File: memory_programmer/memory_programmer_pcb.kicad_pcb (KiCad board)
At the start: 2 copper layers, 68.6 x 53.3 mm, 22 parts, among them J1 Conn_01x03, J2 Conn_02x08_Odd_Even, J3 Conn_02x08_Odd_Even, P1 Power, P2 Analog, P3 Digital, P4 Digital, P5 CONN_01X01, P6 CONN_01X01, P7 CONN_01X01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

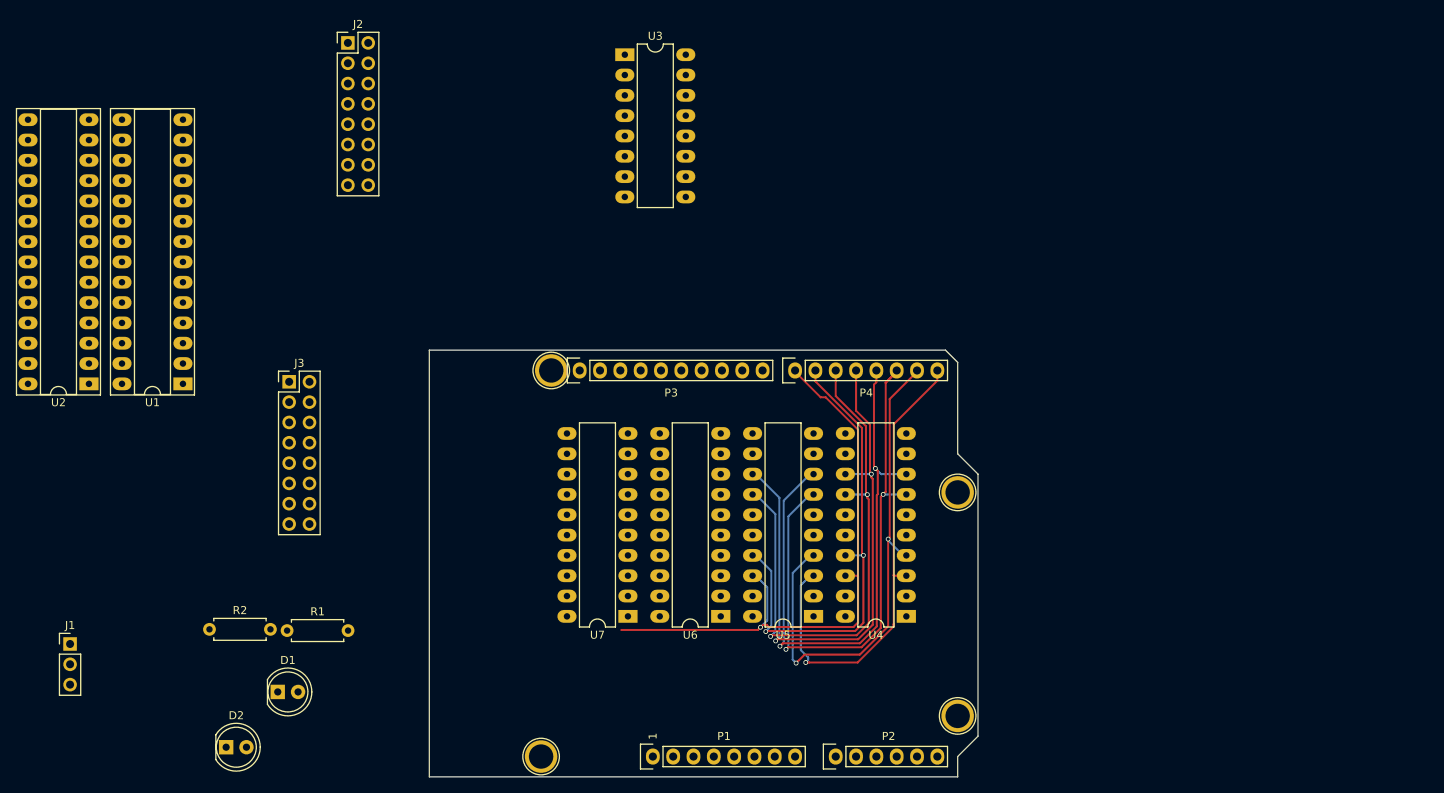
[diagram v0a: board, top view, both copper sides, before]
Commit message: memory programmer and cu
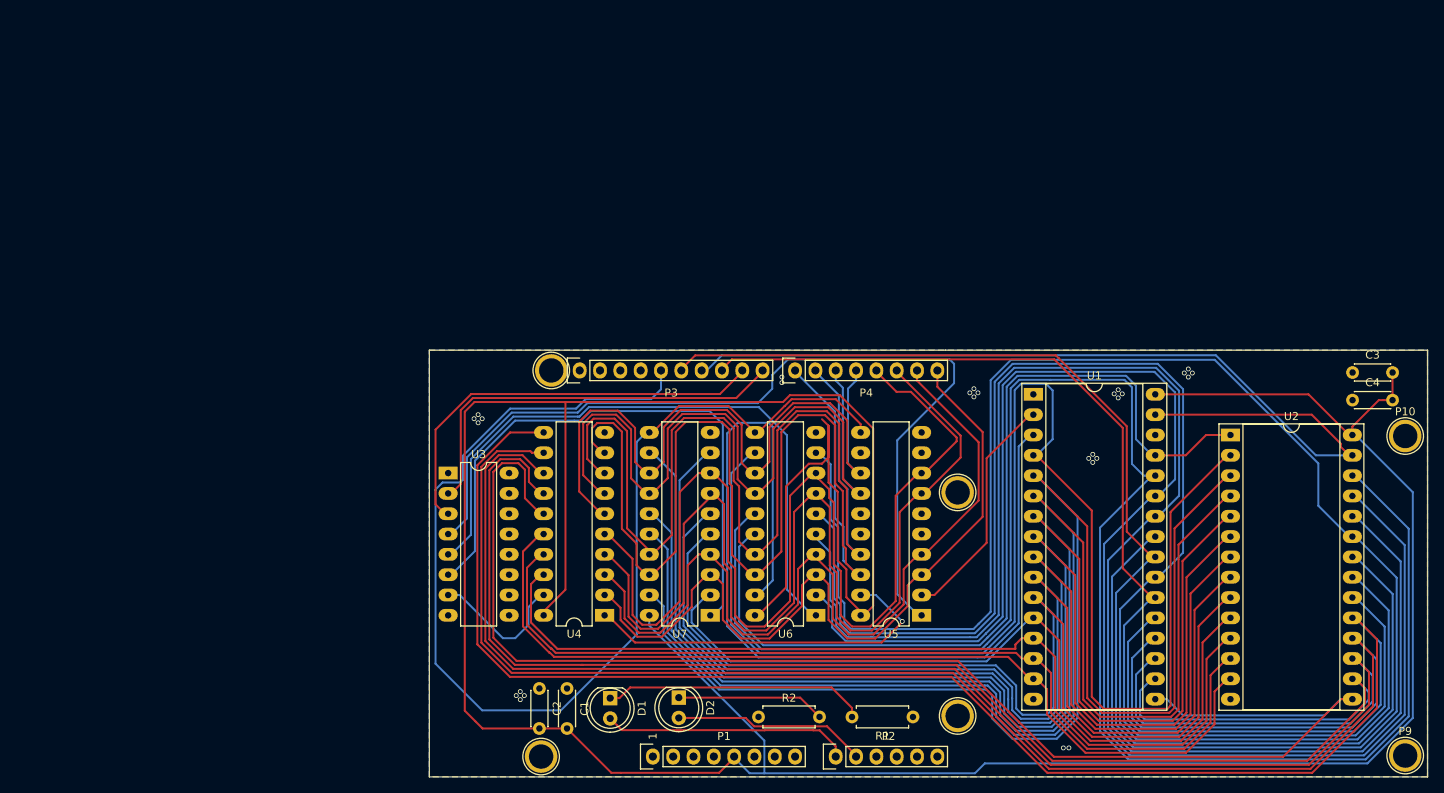
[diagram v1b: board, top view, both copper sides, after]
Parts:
- removed J1: Conn_01x03, Connector_PinHeader_2.54mm:PinHeader_1x03_P2.54mm_Vertical
- removed J2, J3: Conn_02x08_Odd_Even, Connector_PinHeader_2.54mm:PinHeader_2x08_P2.54mm_Vertical
- added C1: 0.1µF, Capacitor_THT:C_Disc_D4.3mm_W1.9mm_P5.00mm, F.Cu at (128.2, 115.3)
- added C2: 0.1µF, Capacitor_THT:C_Disc_D4.3mm_W1.9mm_P5.00mm, F.Cu at (124.8, 115.3)
- added C3: 0.1µF, Capacitor_THT:C_Disc_D4.3mm_W1.9mm_P5.00mm, F.Cu at (226.4, 75.8)
- added C4: 0.1µF, Capacitor_THT:C_Disc_D4.3mm_W1.9mm_P5.00mm, F.Cu at (226.4, 79.3)
- added P10: CONN_01X01, Socket_Arduino_Uno:Arduino_1pin, F.Cu at (233.0, 83.8)
- added P9: CONN_01X01, Socket_Arduino_Uno:Arduino_1pin, F.Cu at (233.0, 123.7)
- U1: value AT28C256-15PU -> SST39SF010; footprint Package_DIP:DIP-28_W7.62mm_Socket_LongPads -> Package_DIP:DIP-32_W15.24mm_Socket_LongPads
- U2: footprint Package_DIP:DIP-28_W7.62mm_Socket_LongPads -> Package_DIP:DIP-28_W15.24mm_Socket_LongPads
- U4: value 74LS377 -> 74LS245
- moved U2 142.8 mm to (211.1, 83.6), turned to 0 degrees
- moved U1 106.3 mm to (186.5, 78.5), turned to 0 degrees
- moved R1 79.0 mm to (171.4, 118.9), turned to 180 degrees
- moved R2 69.5 mm to (152.1, 118.9)
- moved D2 56.9 mm to (142.2, 116.5), turned to 270 degrees
- moved U3 56.8 mm to (113.3, 88.4)
- moved D1 41.6 mm to (133.6, 116.5), turned to 270 degrees
- moved U4 37.7 mm to (132.9, 106.2)
- moved U5 13.5 mm to (172.5, 106.2)
- moved U6 11.9 mm to (159.3, 106.2)
- moved U7 10.3 mm to (146.1, 106.2)
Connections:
- U1 pad 1: /memory/AD14 -> Net-(U1-Pad1)
- U1 pad 10: /memory/AD0 -> /memory/AD2
- U1 pad 11: /data out/D8 -> /memory/AD1
- U1 pad 12: /data out/D9 -> /memory/AD0
- U1 pad 13: /data out/D10 -> /memory/D0
- U1 pad 14: GND -> /memory/D1
- U1 pad 15: /data out/D11 -> /memory/D2
- U1 pad 16: /data out/D12 -> GND
- U1 pad 17: /data out/D13 -> /memory/D3
- U1 pad 18: /data out/D14 -> /memory/D4
- U1 pad 19: /data out/D15 -> /memory/D5
- U1 pad 2: /memory/AD12 -> /memory/AD16
- U1 pad 20: /10(**/SS) -> /memory/D6
- U1 pad 21: /memory/AD10 -> /memory/D7
- U1 pad 22: /12(MISO) -> /10(**/SS)
- U1 pad 23: /memory/AD11 -> /memory/AD10
- U1 pad 24: /memory/AD9 -> /12(MISO)
- U1 pad 25: /memory/AD8 -> /memory/AD11
- U1 pad 26: /memory/AD13 -> /memory/AD9
- U1 pad 27: /11(**/MOSI) -> /memory/AD8
- U1 pad 28: +5V -> /memory/AD13
- U1 pad 3: /memory/AD7 -> /memory/AD15
- U1 pad 4: /memory/AD6 -> /memory/AD12
- U1 pad 5: /memory/AD5 -> /memory/AD7
- U1 pad 6: /memory/AD4 -> /memory/AD6
- U1 pad 7: /memory/AD3 -> /memory/AD5
- U1 pad 8: /memory/AD2 -> /memory/AD4
- U1 pad 9: /memory/AD1 -> /memory/AD3
- U2 pad 11: /data out/D0 -> /memory/D0
- U2 pad 12: /data out/D1 -> /memory/D1
- U2 pad 13: /data out/D2 -> /memory/D2
- U2 pad 15: /data out/D3 -> /memory/D3
- U2 pad 16: /data out/D4 -> /memory/D4
- U2 pad 17: /data out/D5 -> /memory/D5
- U2 pad 18: /data out/D6 -> /memory/D6
- U2 pad 19: /data out/D7 -> /memory/D7
- U4 pad 1: Net-(U3-Pad7) -> Net-(U4-Pad1)
- U4 pad 11: /13(SCK) -> /memory/D7
- U4 pad 12: /data out/D12 -> /memory/D6
- U4 pad 13: /4 -> /memory/D5
- U4 pad 14: /5(**) -> /memory/D4
- U4 pad 15: /data out/D13 -> /memory/D3
- U4 pad 16: /data out/D14 -> /memory/D2
- U4 pad 17: /6(**) -> /memory/D1
- U4 pad 18: /7 -> /memory/D0
- U4 pad 19: /data out/D15 -> Net-(U3-Pad7)
- U4 pad 2: /data out/D8 -> /0(Rx)
- U4 pad 3: /0(Rx) -> /1(Tx)
- U4 pad 4: /1(Tx) -> /2
- U4 pad 5: /data out/D9 -> /3(**)
- U4 pad 6: /data out/D10 -> /4
- U4 pad 7: /2 -> /5(**)
- U4 pad 8: /3(**) -> /6(**)
- U4 pad 9: /data out/D11 -> /7
- U5 pad 1: Net-(U3-Pad6) -> Net-(U3-Pad4)
- U5 pad 12: /data out/D4 -> Net-(U5-Pad12)
- U5 pad 15: /data out/D5 -> Net-(U5-Pad15)
- U5 pad 16: /data out/D6 -> Net-(U5-Pad16)
- U5 pad 19: /data out/D7 -> Net-(U4-Pad1)
- U5 pad 2: /data out/D0 -> /memory/AD16
- U5 pad 5: /data out/D1 -> Net-(U5-Pad5)
- U5 pad 6: /data out/D2 -> Net-(U5-Pad6)
- U5 pad 9: /data out/D3 -> Net-(U5-Pad9)
- U7 pad 1: Net-(U3-Pad4) -> Net-(U3-Pad6)
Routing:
- net +5V: track 0.00 -> 426.8 mm
- net /memory/D7: track 0.00 -> 228.1 mm
- net /memory/AD13: track 0.00 -> 220.8 mm
- net /memory/AD11: track 0.00 -> 219.0 mm
- net /memory/D6: track 0.00 -> 215.1 mm
- net /memory/D5: track 0.00 -> 203.5 mm
- net /memory/AD9: track 0.00 -> 201.6 mm
- net /memory/AD8: track 0.00 -> 198.3 mm
- net /memory/D4: track 0.00 -> 193.2 mm
- net /memory/AD10: track 0.00 -> 190.8 mm
- net /memory/AD12: track 0.00 -> 183.9 mm
- net /memory/D3: track 0.00 -> 175.0 mm
- net /memory/AD7: track 0.00 -> 173.5 mm
- net /memory/AD6: track 0.00 -> 173.1 mm
- net /memory/AD5: track 0.00 -> 167.6 mm
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- added copper zone on B.Cu, net GND
- added copper zone on F.Cu, net GND
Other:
- board size 68.6 x 53.3 mm -> 124.8 x 53.3 mm
